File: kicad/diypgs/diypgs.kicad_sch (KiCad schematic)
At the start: 15 parts, among them SW1 SW_Push_Dual, SW2 SW_Push_Dual, SW3 SW_Push_Dual, SW4 SW_Push_Dual, SW5 SW_Push_Dual, SW6 SW_Push_Dual

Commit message: Add PCB design
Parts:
- R1, R2, R3, R4, R5, R6: footprint (none) -> Resistor_THT:R_Axial_DIN0207_L6.3mm_D2.5mm_P7.62mm_Horizontal
- SW1, SW2, SW3, SW4, SW5, SW6: footprint (none) -> Button_Switch_THT:SW_PUSH_6mm
- U1: value (none) -> Nokia_5110_LCD; footprint (none) -> Nokia_5110-3310_LCD:Nokia_5110-3310_LCD
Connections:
- net +3V3: now also SW1.2; no longer SW1.1
- net at R1.1: now also SW1.1; no longer SW1.3
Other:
- moved on the sheet: R1

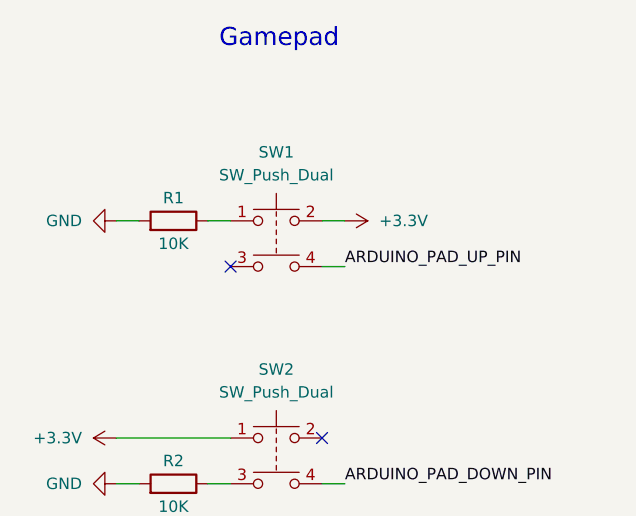
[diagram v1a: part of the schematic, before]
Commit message: Fix button pad number
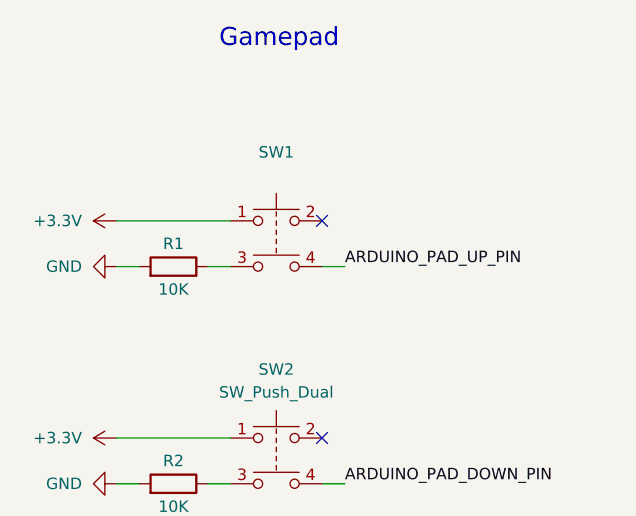
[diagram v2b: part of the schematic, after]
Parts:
- SW1: value SW_Push_Dual -> (none); footprint Button_Switch_THT:SW_PUSH_6mm -> (none)
- SW2, SW3, SW4, SW5, SW6: footprint Button_Switch_THT:SW_PUSH_6mm -> (none)
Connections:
- net +3V3: now also SW1.1; no longer SW1.2
- net at R1.1: now also SW1.3; no longer SW1.1
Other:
- moved on the sheet: R1

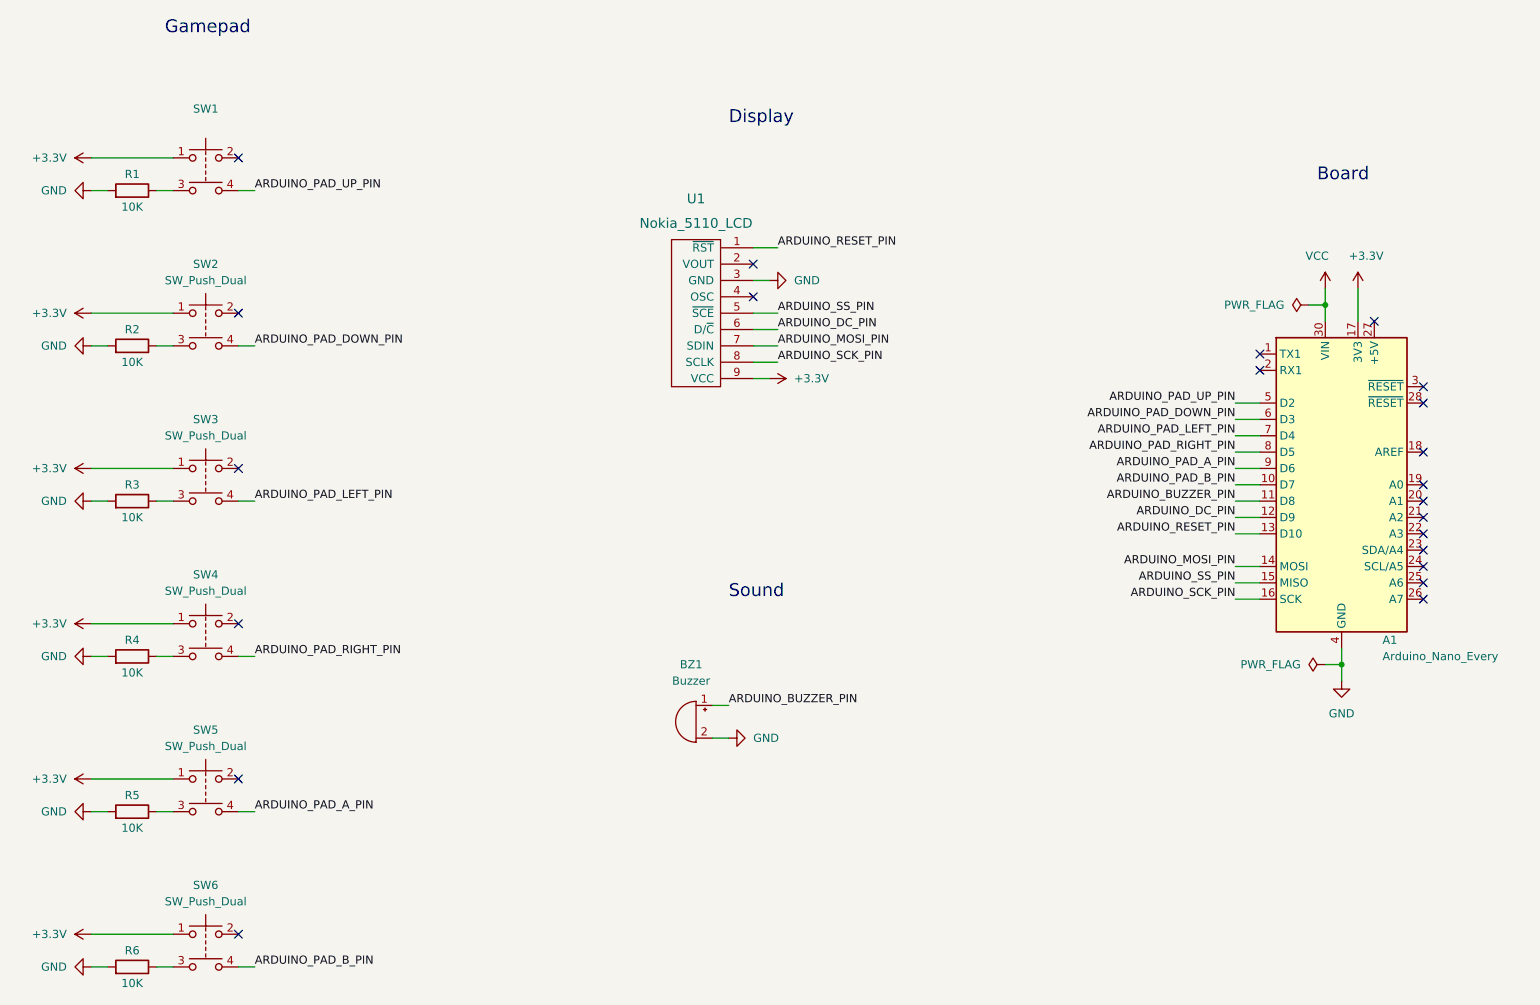
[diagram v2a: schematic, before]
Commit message: Add PCB tracks
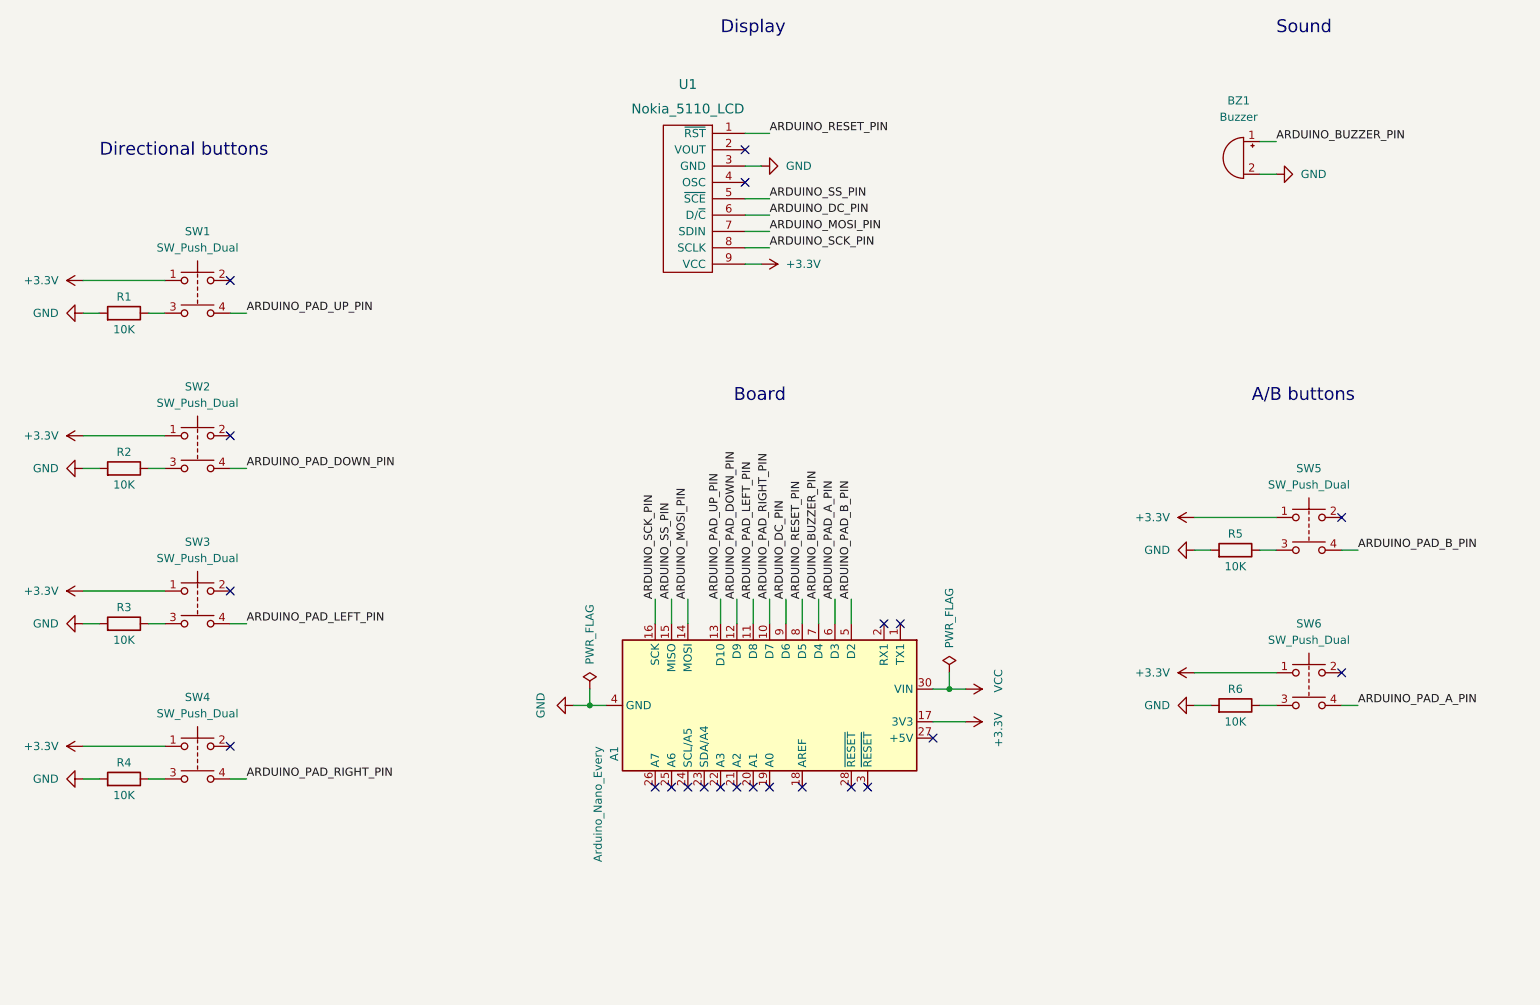
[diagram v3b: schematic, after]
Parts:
- SW1: value (none) -> SW_Push_Dual; footprint (none) -> Footprints:SW_PUSH_6mm_ALT
- SW2, SW3, SW4, SW5, SW6: footprint (none) -> Footprints:SW_PUSH_6mm_ALT
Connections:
- net ARDUINO_BUZZER_PIN: now also A1.7 (D4); no longer A1.11 (D8)
- net ARDUINO_DC_PIN: now also A1.9 (D6); no longer A1.12 (D9)
- net ARDUINO_PAD_A_PIN: now also A1.6 (D3), SW6.4; no longer A1.9 (D6), SW5.4
- net ARDUINO_PAD_B_PIN: now also A1.5 (D2), SW5.4; no longer A1.10 (D7), SW6.4
- net ARDUINO_PAD_DOWN_PIN: now also A1.12 (D9); no longer A1.6 (D3)
- net ARDUINO_PAD_LEFT_PIN: now also A1.11 (D8); no longer A1.7 (D4)
- net ARDUINO_PAD_RIGHT_PIN: now also A1.10 (D7); no longer A1.8 (D5)
- net ARDUINO_PAD_UP_PIN: now also A1.13 (D10); no longer A1.5 (D2)
- net ARDUINO_RESET_PIN: now also A1.8 (D5); no longer A1.13 (D10)
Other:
- note added: "A/B buttons"
- note added: "Directional buttons"
- note removed: "Gamepad"
- moved on the sheet: A1, BZ1, R1, R2, R3, R4, R5, R6, SW1, SW2, SW3, SW4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

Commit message: Fix screen symbol and footprint
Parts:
- removed U1: Nokia_5110_LCD, Nokia_5110-3310_LCD:Nokia_5110-3310_LCD, symbol nokia_5110-3310_lcd:Nokia_5110_LCD
- added U1: Sparkfun - Graphic LCD 84x48 - Nokia 5110, Footprints:Sparkfun - Graphic LCD 84x48 - Nokia 5110, symbol Symbols:Sparkfun - Graphic LCD 84x48 - Nokia 5110
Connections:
- net +3V3: now also U1.1 (VCC)
- net ARDUINO_DC_PIN: now also A1.8 (D5), U1.5 (D/~{C}); no longer A1.9 (D6)
- net ARDUINO_MOSI_PIN: now also U1.6 (MOSI)
- net ARDUINO_RESET_PIN: now also A1.9 (D6), U1.4 (~{RST}); no longer A1.8 (D5)
- net ARDUINO_SCK_PIN: now also U1.7 (SCLK)
- net ARDUINO_SS_PIN: now also U1.3 (~{SCE})
- net GND: now also U1.2 (GND)
- no-connect marks 22 -> 20

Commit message: All tracks routed
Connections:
- net +3V3: now also SW1.3, SW2.3, SW3.3, SW4.3; no longer SW1.1, SW2.1, SW3.1, SW4.1
- net ARDUINO_PAD_DOWN_PIN: now also A1.10 (D7), SW2.2; no longer A1.12 (D9), SW2.4
- net ARDUINO_PAD_LEFT_PIN: now also SW3.2; no longer SW3.4
- net ARDUINO_PAD_RIGHT_PIN: now also A1.12 (D9), SW4.2; no longer A1.10 (D7), SW4.4
- net ARDUINO_PAD_UP_PIN: now also SW1.2; no longer SW1.4
- net at R4.1: now also SW4.1; no longer SW4.3
- net at R2.1: now also SW2.1; no longer SW2.3
- net at R1.1: now also SW1.1; no longer SW1.3
- net at R3.1: now also SW3.1; no longer SW3.3
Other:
- moved on the sheet: R1, R2, R3, R4

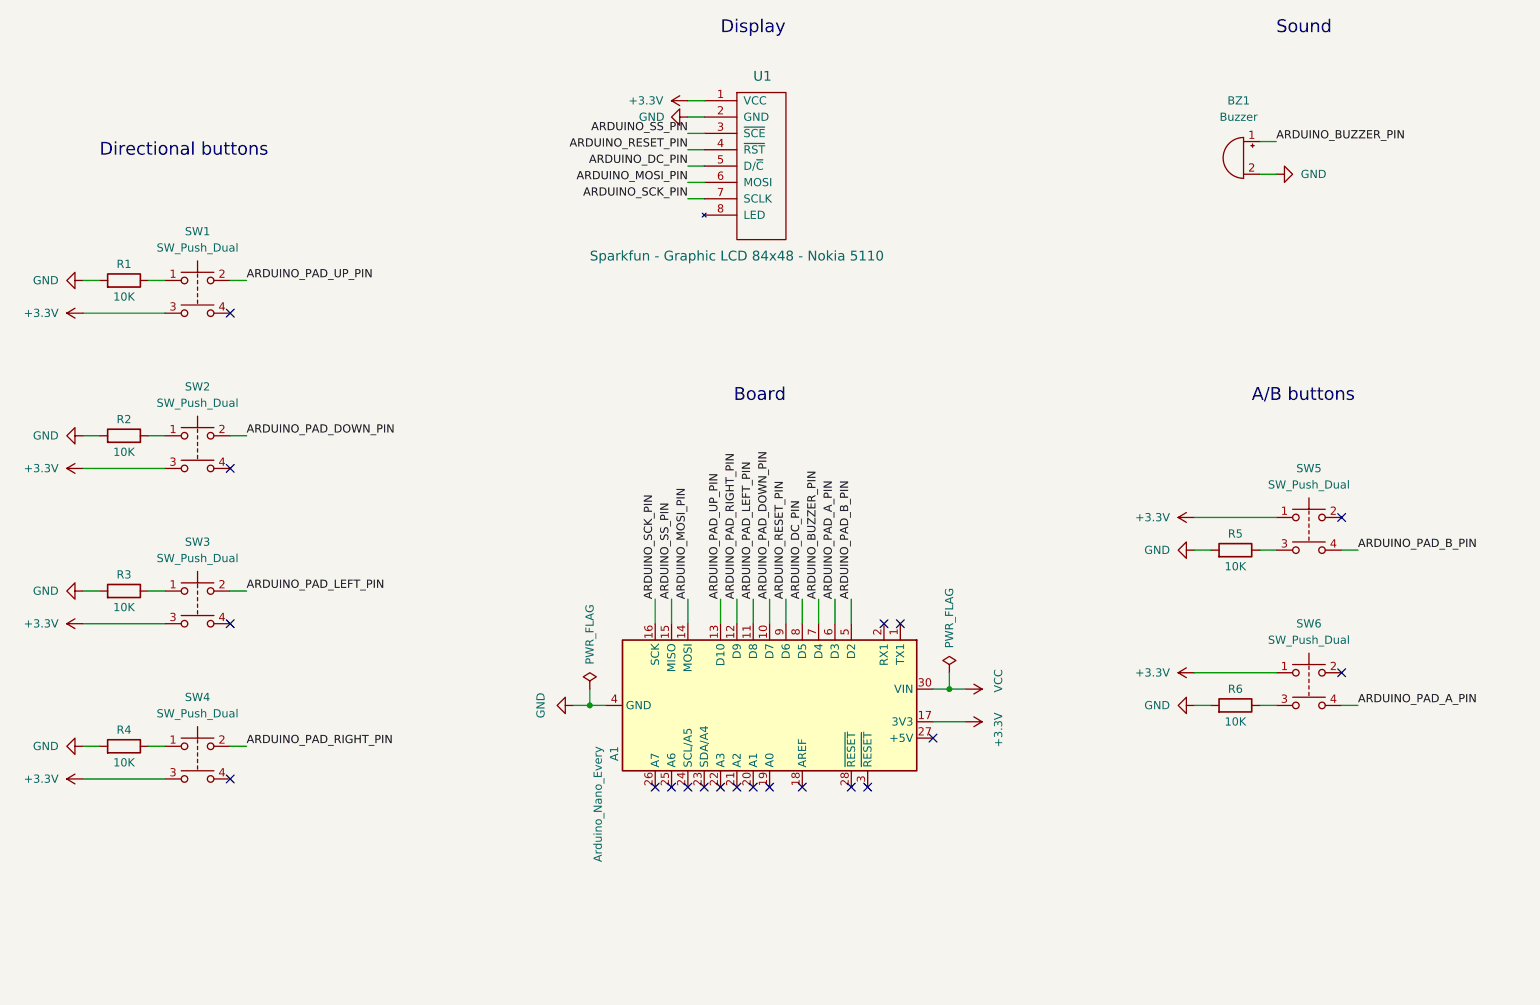
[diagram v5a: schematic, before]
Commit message: Add JST connector
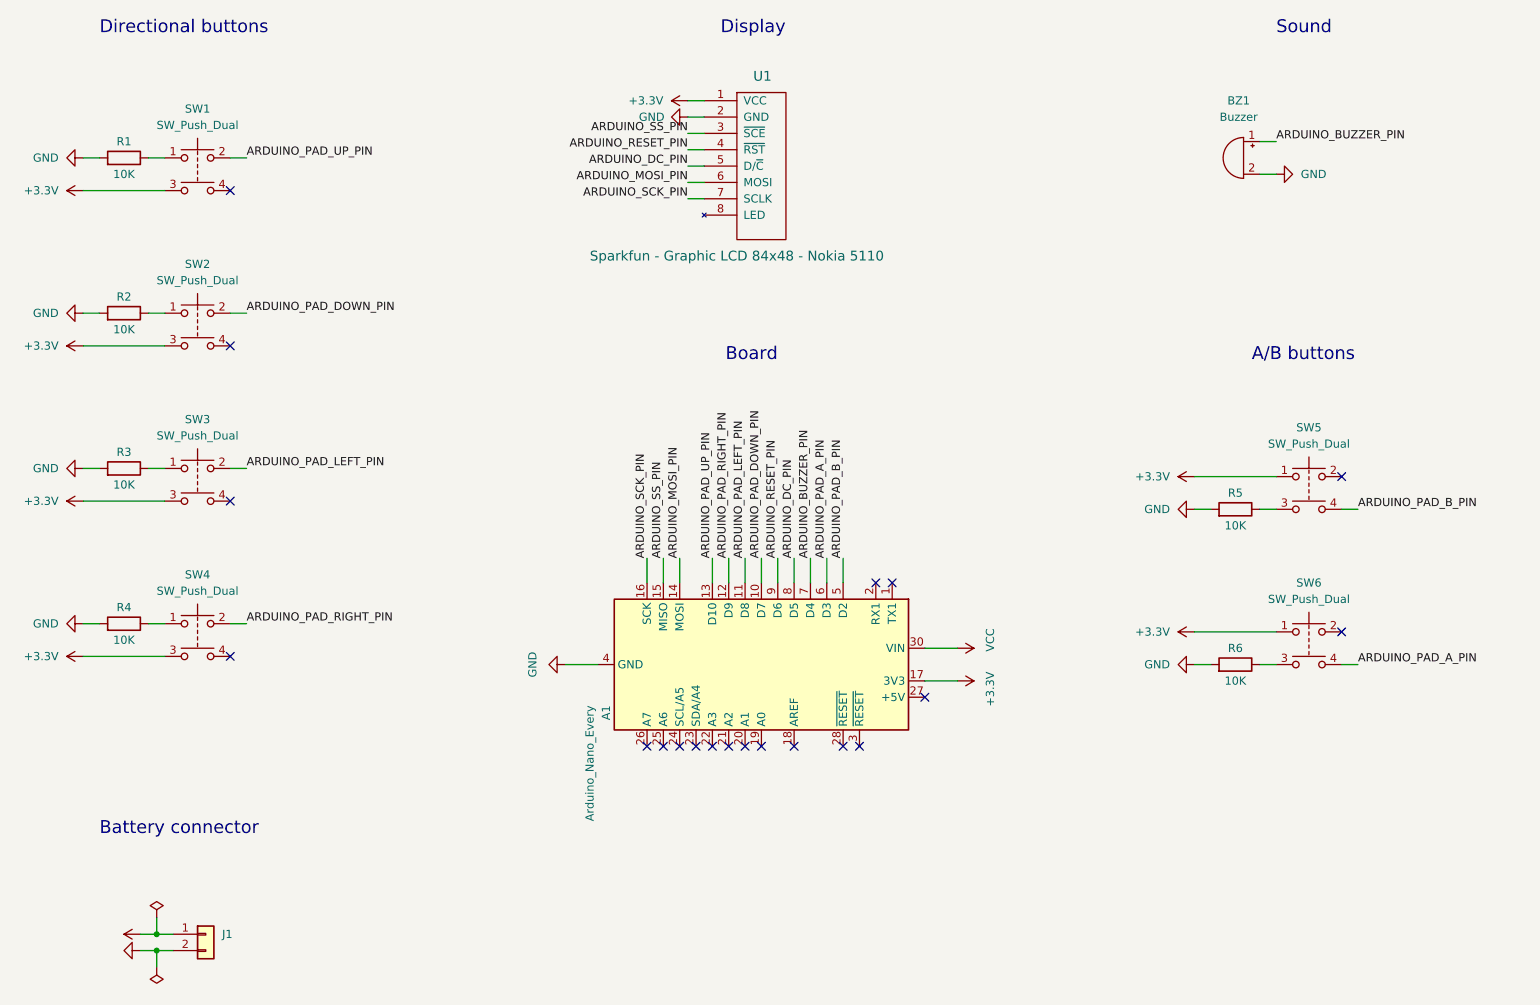
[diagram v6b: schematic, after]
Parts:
- added J1: (no value), symbol Connector_Generic:Conn_01x02
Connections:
- net GND: now also J1.2 (Pin_2)
- net VCC: now also J1.1 (Pin_1)
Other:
- note added: "Battery connector"
- moved on the sheet: A1, R1, R2, R3, R4, R5, R6, SW1, SW2, SW3, SW4, SW5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
